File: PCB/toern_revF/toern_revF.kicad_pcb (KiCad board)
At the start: 4 copper layers, 160 x 71 mm, 92 parts, among them J1 AudioJack3_Switch, J10 Conn_01x02, J11 Conn_01x05, J11.5 Conn_01x05, J12 Conn_01x05, J13 Conn_01x05, J14 Conn_01x05, J15 Conn_01x05, J16 BATTERY, J17 AudioJack3_Ground, J3 AudioJack3_Ground, J4 USB_C_Receptacle_USB2.0, J5 AudioJack3_Switch, J6 AudioJack3_Switch, J7 AudioJack3_Switch, J8 Micro_SD_Card, J9 Conn_01x03, Q1 DMG3415, SW1 EG2219, U1 SPX3819M5-L-3-3, U10 01x05 Connector_PinSocket_2.5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, U11 01x05 Connector_PinSocket_2.5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, U12 01x05 Connector_PinSocket_2.5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, U13 PAM8403D, U2 SPX3819M5-L-1-8, U3 SGTL5000XNBA3, U4 TLP2361V4_E, U5 74LVC2G14, U6 Teensy4.1, U7 SPX3819M5-L-3-3, U8 MCP73831-3-OT, U9 01x05 Connector_PinSocket_2.5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

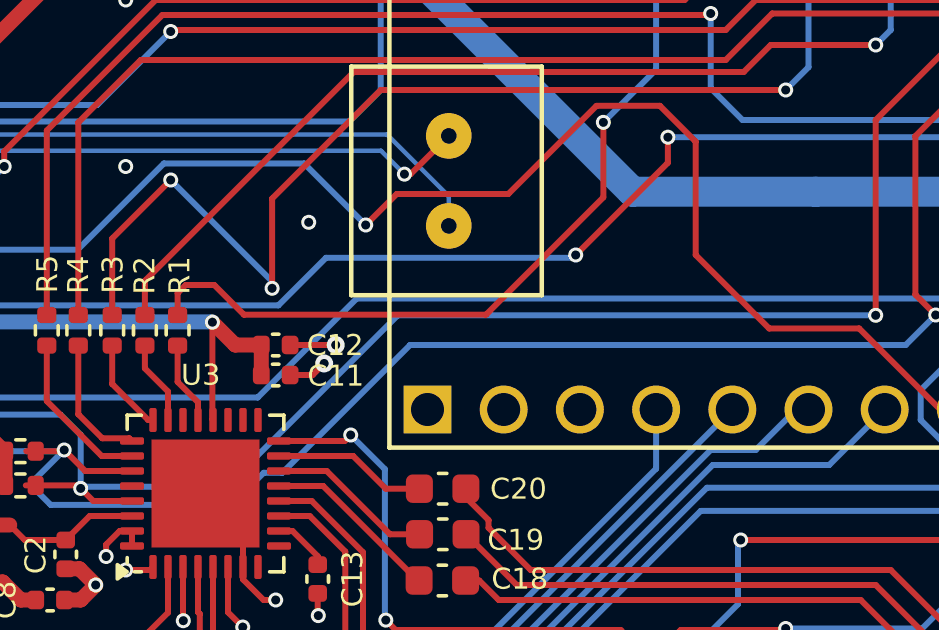
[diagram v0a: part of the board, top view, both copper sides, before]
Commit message: clean up kiCad Files
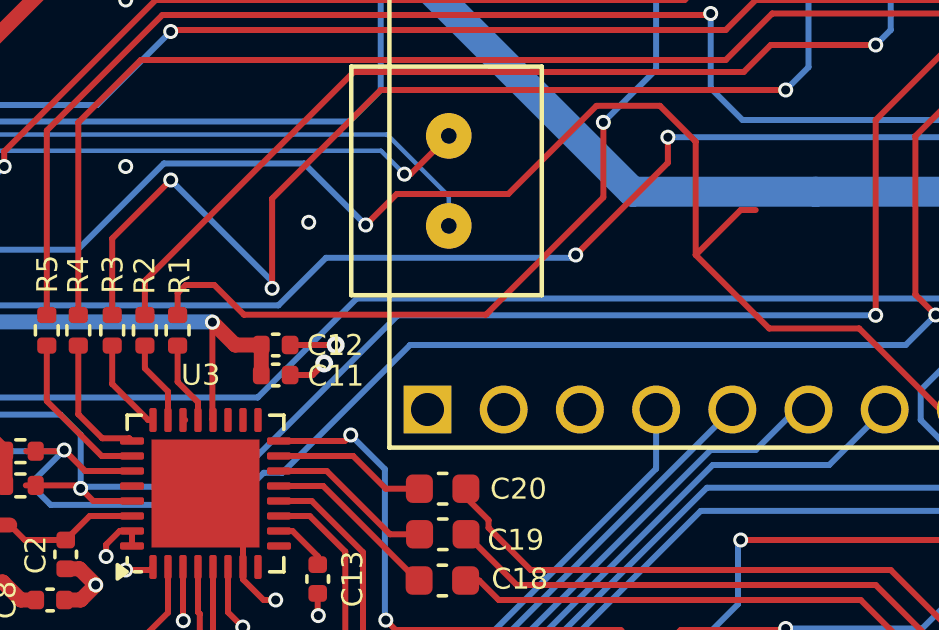
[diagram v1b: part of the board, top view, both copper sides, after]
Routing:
- net 6_OUT1D: track 63.4 -> 66.0 mm
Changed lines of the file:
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@@
+	)
+	(segment
+		(start 107.41 42.5)
+		(end 107.484 42.5)
+		(width 0.2)
+		(layer "F.Cu")
+		(net 84)
 	)
 	(segment
@@
 		(width 0.2)
 		(layer "F.Cu")
+		(net 90)
+	)
+	(segment
+		(start 126 35.5)
+		(end 126.5 35.5)
+		(width 0.2)
+		(layer "F.Cu")
+		(net 90)
+	)
+	(segment
+		(start 124.5 37)
+		(end 126 35.5)
+		(width 0.2)
+		(layer "F.Cu")
